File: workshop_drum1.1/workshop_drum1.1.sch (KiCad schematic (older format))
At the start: 30 parts, among them J1 9v_Battery_Clip, J2 Trigger_Input, J3 Output, U1 LM358, U2 7414, U3 78L05

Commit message: P1.1 - Updated footprints prior to deleting PCB
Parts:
- removed C?: 10uF, 4ms-footprints:Cap_Electrolytic_TH, symbol 4ms-passives:CAP-ELEC-TH
- removed SW?: SPDT_small, zfoot:Switch_Toggle_SPDT_Mini_SolderLug, symbol zMECH:SPDT_small
- added EnvelopeAndVoltageStarve1: PWRStrip, zfoot:BreadBoardStrip_4, symbol zMECH:GNDStrip
- added GND1: GNDStrip, zfoot:BreadBoardStripBold_4, symbol zMECH:GNDStrip
- added GND2: GNDStrip, zfoot:BreadBoardStripBold_7, symbol zMECH:GNDStrip
- added IN1, IN2, IN3, OUT1, OUT2, OUT3, PathToSwitch1: BreadBoardStrip, zfoot:BreadBoardStrip_4, symbol zMECH:BreadBoardStrip
- added Osc_Select1: SPDT_small, zfoot:Switch_Toggle_SPDT_Mini_SolderLug, symbol zMECH:SPDT_small
- added R10: 470 after pot on output, 4ms-footprints:Resistor_TH_300, symbol 4ms-passives:RTH
- added R9: 1k - trig input resistor, 4ms-footprints:Resistor_TH_300, symbol 4ms-passives:RTH
- C2: value 1uF -> 1uF or smaller?
- C5: value 220nF -> 100nf-220nF or bigger?
- DECAY1: value A500k-A1M -> A100k-A1M
- J2, J3: footprint zfoot:Jack_Instrument_Bigger -> zfoot:Jack_Instrument
- ON/OFF_LED1, Trig_LED1: footprint zfoot:LED_D5.0mm -> zfoot:LED_wired
- PITCH1: value B50k -> B50k- try with A100k
- R3: value 1k -> 1k smaller is brighter
- R4: value 1M -> SET THIS TO ADJUST SENSE
- R5: value 100k -> 100k before decay pot
- R6: value 470 -> 470 before pot on non-inv input
- R8: value 470 -> 470 smaller is brighter
- SENSE/STARVE1: value A50k -> A100k or bigger
- renumbered Button1 to Switch_On1
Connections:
- wire segments 63 -> 70
- no-connect marks 8 -> 2
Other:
- moved on the sheet: C2, C5, J3, R1, R7, Switch_On1, U1B

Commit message: P1.1 started working on breadboard strip
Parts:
- ON/OFF_LED1, Trig_LED1: footprint zfoot:LED_wired -> zfoot:LED_D5.0mm
- Switch_On1: footprint zfoot:SPST_Wired -> zfoot:Jack_Instrument_Bigger
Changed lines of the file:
@@
 F 0 "ON/OFF_LED1" H 2300 3496 45  0000 C CNN
 F 1 "LED-C1-A2" H 2300 3580 45  0000 C CNN
-F 2 "zfoot:LED_wired" H 2280 3850 20  0001 C CNN
+F 2 "zfoot:LED_D5.0mm" H 2280 3850 20  0001 C CNN
 F 3 "" H 2250 3700 60  0001 C CNN
 	1    2250 3700
@@
 F 0 "Switch_On1" H 1150 1100 60  0000 C CNN
 F 1 "SPST_small" H 1150 1050 20  0000 C CNN
-F 2 "zfoot:SPST_Wired" H 1150 1150 60  0001 C CNN
+F 2 "zfoot:Jack_Instrument_Bigger" H 1150 1150 60  0001 C CNN
 F 3 "" H 1150 1150 60  0001 C CNN
 	1    1150 1150
@@
 F 0 "Trig_LED1" H 6650 2596 45  0000 C CNN
 F 1 "LED-C1-A2" H 6650 2680 45  0000 C CNN
-F 2 "zfoot:LED_wired" H 6630 2950 20  0001 C CNN
+F 2 "zfoot:LED_D5.0mm" H 6630 2950 20  0001 C CNN
 F 3 "" H 6600 2800 60  0001 C CNN
 	1    6600 2800

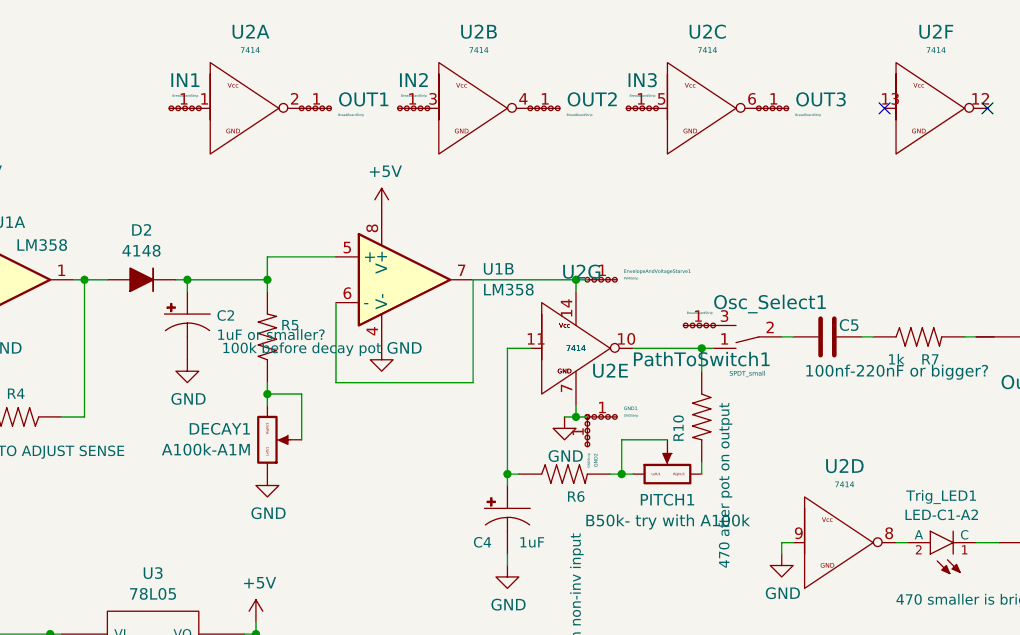
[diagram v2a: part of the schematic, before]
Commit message: re organizing boards with breakout footprints
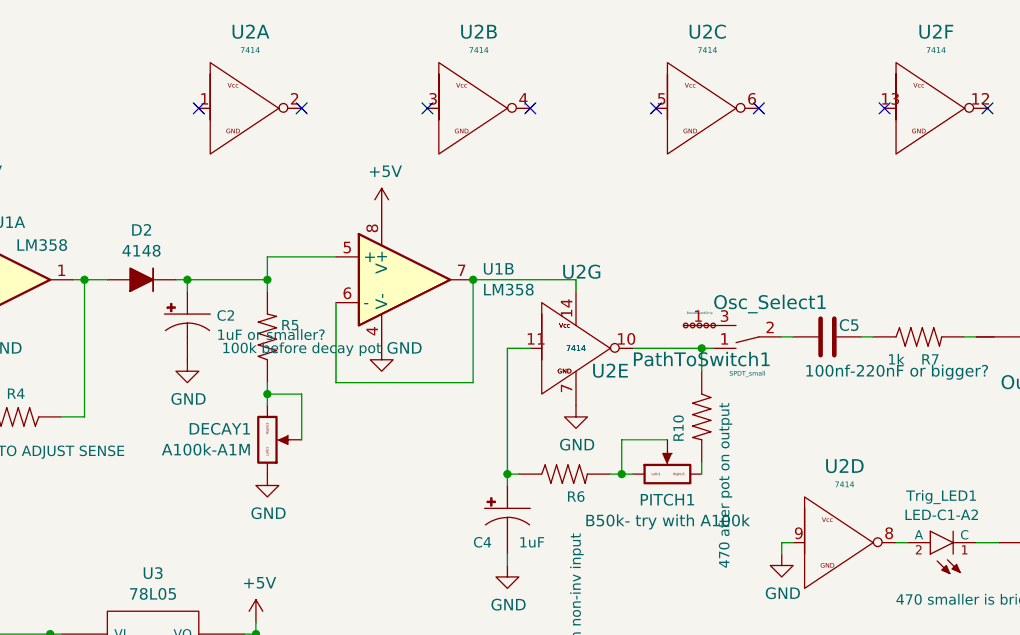
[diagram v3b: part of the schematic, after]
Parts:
- removed EnvelopeAndVoltageStarve1: PWRStrip, zfoot:BreadBoardStrip_4, symbol zMECH:GNDStrip
- removed GND1: GNDStrip, zfoot:BreadBoardStripBold_4, symbol zMECH:GNDStrip
- removed GND2: GNDStrip, zfoot:BreadBoardStripBold_7, symbol zMECH:GNDStrip
- removed IN1, IN2, IN3, OUT1, OUT2, OUT3: BreadBoardStrip, zfoot:BreadBoardStrip_4, symbol zMECH:BreadBoardStrip
- PathToSwitch1: footprint zfoot:BreadBoardStrip_4 -> zfoot:BREAKOUTswitch
- U2: footprint 4ms-footprints:DIP-14_W7.62mm -> zfoot:BREAKOUT
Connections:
- no-connect marks 2 -> 8
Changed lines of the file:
@@
 F 0 "U2" H 5100 1850 60  0000 C CNN
 F 1 "7414" H 4950 1950 25  0000 C CNN
-F 2 "4ms-footprints:DIP-14_W7.62mm" H 4900 2600 60  0001 C CNN
+F 2 "zfoot:BREAKOUT" H 4900 2600 60  0001 C CNN
 F 3 "" H 4900 2600 60  0001 C CNN
 	5    4950 1950
@@
 F 0 "U2" H 6125 3133 60  0000 C CNN
 F 1 "7414" H 6125 3054 25  0000 C CNN
-F 2 "4ms-footprints:DIP-14_W7.62mm" H 6050 3450 60  0001 C CNN
+F 2 "zfoot:BREAKOUT" H 6050 3450 60  0001 C CNN
 F 3 "" H 6050 3450 60  0001 C CNN
 	4    6100 2800
@@
 F 0 "U2" H 3525 1233 60  0000 C CNN
 F 1 "7414" H 3525 1154 25  0000 C CNN
-F 2 "4ms-footprints:DIP-14_W7.62mm" H 3450 1550 60  0001 C CNN
+F 2 "zfoot:BREAKOUT" H 3450 1550 60  0001 C CNN
 F 3 "" H 3450 1550 60  0001 C CNN
 	1    3500 900
@@
 F 0 "U2" H 5525 1233 60  0000 C CNN
 F 1 "7414" H 5525 1154 25  0000 C CNN
-F 2 "4ms-footprints:DIP-14_W7.62mm" H 5450 1550 60  0001 C CNN
+F 2 "zfoot:BREAKOUT" H 5450 1550 60  0001 C CNN
 F 3 "" H 5450 1550 60  0001 C CNN
 	3    5500 900
@@
 F 0 "U2" H 4525 1233 60  0000 C CNN
 F 1 "7414" H 4525 1154 25  0000 C CNN
-F 2 "4ms-footprints:DIP-14_W7.62mm" H 4450 1550 60  0001 C CNN
+F 2 "zfoot:BREAKOUT" H 4450 1550 60  0001 C CNN
 F 3 "" H 4450 1550 60  0001 C CNN
 	2    4500 900
@@
 F 0 "U2" H 6525 1233 60  0000 C CNN
 F 1 "7414" H 6525 1154 25  0000 C CNN
-F 2 "4ms-footprints:DIP-14_W7.62mm" H 6450 1550 60  0001 C CNN
+F 2 "zfoot:BREAKOUT" H 6450 1550 60  0001 C CNN
 F 3 "" H 6450 1550 60  0001 C CNN
 	6    6500 900
-	1    0    0    -1
-$EndComp
-$Comp
-L zMECH:BreadBoardStrip IN1
-U 1 1 5A32DFC0
-P 3300 900
-F 0 "IN1" H 3359 779 60  0000 C CNN
-F 1 "BreadBoardStrip" H 3359 845 10  0000 C CNN
-F 2 "zfoot:BreadBoardStrip_4" H 3170 880 60  0001 C CNN
-F 3 "" H 3300 900 60  0001 C CNN
-	1    3300 900
-	-1   0    0    1
-$EndComp
-$Comp
-L zMECH:BreadBoardStrip OUT1
-U 1 1 5A32E0DC
-P 3750 900
-F 0 "OUT1" H 3909 937 60  0000 L CNN
-F 1 "BreadBoardStrip" H 3909 871 10  0000 L CNN
-F 2 "zfoot:BreadBoardStrip_4" H 3620 880 60  0001 C CNN
-F 3 "" H 3750 900 60  0001 C CNN
-	1    3750 900
-	1    0    0    -1
-$EndComp
-$Comp
-L zMECH:BreadBoardStrip OUT3
-U 1 1 5A32E1BF
-P 5750 900
-F 0 "OUT3" H 5909 937 60  0000 L CNN
-F 1 "BreadBoardStrip" H 5909 871 10  0000 L CNN
-F 2 "zfoot:BreadBoardStrip_4" H 5620 880 60  0001 C CNN
-F 3 "" H 5750 900 60  0001 C CNN
-	1    5750 900
-	1    0    0    -1
-$EndComp
-$Comp
-L zMECH:BreadBoardStrip OUT2
-U 1 1 5A32E1FA
-P 4750 900
-F 0 "OUT2" H 4909 937 60  0000 L CNN
-F 1 "BreadBoardStrip" H 4909 871 10  0000 L CNN
-F 2 "zfoot:BreadBoardStrip_4" H 4620 880 60  0001 C CNN
-F 3 "" H 4750 900 60  0001 C CNN
-	1    4750 900
-	1    0    0    -1
-$EndComp
-$Comp
-L zMECH:BreadBoardStrip IN2
-U 1 1 5A32E61E
-P 4300 900
-F 0 "IN2" H 4359 779 60  0000 C CNN
-F 1 "BreadBoardStrip" H 4359 845 10  0000 C CNN
-F 2 "zfoot:BreadBoardStrip_4" H 4170 880 60  0001 C CNN
-F 3 "" H 4300 900 60  0001 C CNN
-	1    4300 900
-	-1   0    0    1
-$EndComp
-$Comp
-L zMECH:BreadBoardStrip IN3
-U 1 1 5A32E6B1
-P 5300 900
-F 0 "IN3" H 5359 779 60  0000 C CNN
-F 1 "BreadBoardStrip" H 5359 845 10  0000 C CNN
-F 2 "zfoot:BreadBoardStrip_4" H 5170 880 60  0001 C CNN
-F 3 "" H 5300 900 60  0001 C CNN
-	1    5300 900
-	-1   0    0    1
-$EndComp
-$Comp
-L zMECH:GNDStrip GND1
-U 1 1 5A32F5DA
-P 5000 2250
-F 0 "GND1" H 5159 2287 15  0000 L CNN
-F 1 "GNDStrip" H 5159 2256 10  0000 L CNN
-F 2 "zfoot:BreadBoardStripBold_4" H 4870 2230 60  0001 C CNN
-F 3 "" H 5000 2250 60  0001 C CNN
-	1    5000 2250
 	1    0    0    -1
 $EndComp
@@
 F 0 "U2" H 4975 2283 60  0000 C CNN
 F 1 "7414" H 4950 1950 25  0000 C CNN
-F 2 "4ms-footprints:DIP-14_W7.62mm" H 4900 2600 60  0001 C CNN
+F 2 "zfoot:BREAKOUT" H 4900 2600 60  0001 C CNN
 F 3 "" H 4900 2600 60  0001 C CNN
 	7    4950 1950
@@
 $EndComp
 Wire Wire Line
-	4950 1700 4950 1650
-Wire Wire Line
-	4500 1650 4950 1650
-Wire Wire Line
-	4950 2200 4950 2250
-Wire Wire Line
-	4950 2250 5000 2250
-Wire Wire Line
 	1600 3550 1600 3600
 Wire Wire Line
@@
 Wire Wire Line
 	4500 2100 4500 1650
-Connection ~ 4950 1650
 Wire Wire Line
 	4650 1950 4650 2500
@@
 F 0 "PathToSwitch1" H 5600 2000 60  0000 C CNN
 F 1 "BreadBoardStrip" H 5609 1795 10  0000 C CNN
-F 2 "zfoot:BreadBoardStrip_4" H 5420 1830 60  0001 C CNN
+F 2 "zfoot:BREAKOUTswitch" H 5420 1830 60  0001 C CNN
 F 3 "" H 5550 1850 60  0001 C CNN
 	1    5550 1850
 	-1   0    0    1
 $EndComp
-$Comp
-L zMECH:GNDStrip EnvelopeAndVoltageStarve1
-U 1 1 5A330F13
-P 5000 1650
-F 0 "EnvelopeAndVoltageStarve1" H 5159 1687 15  0000 L CNN
-F 1 "PWRStrip" H 5159 1656 10  0000 L CNN
-F 2 "zfoot:BreadBoardStrip_4" H 4870 1630 60  0001 C CNN
-F 3 "" H 5000 1650 60  0001 C CNN
-	1    5000 1650
-	1    0    0    -1
-$EndComp
 NoConn ~ 6300 900
 NoConn ~ 6750 900
-$Comp
-L zMECH:GNDStrip GND2
-U 1 1 5A336833
-P 5000 2250
-F 0 "GND2" H 5159 2287 15  0000 L CNN
-F 1 "GNDStrip" H 5159 2256 10  0000 L CNN
-F 2 "zfoot:BreadBoardStripBold_7" H 4870 2230 60  0001 C CNN
-F 3 "" H 5000 2250 60  0001 C CNN
-	1    5000 2250
-	0    1    1    0
-$EndComp
 Wire Wire Line
 	2000 3200 2050 3200
@@
 Wire Wire Line
 	3600 1650 3600 1700
-Wire Wire Line
-	4950 1650 5000 1650
 Wire Wire Line
 	4650 2500 4650 2550
@@
 L 4ms-power:GND #PWR0101
 U 1 1 5ABB579D
-P 4900 2250
-F 0 "#PWR0101" H 4900 2000 50  0001 C CNN
-F 1 "GND" H 4905 2077 50  0000 C CNN
-F 2 "" H 4900 2250 50  0001 C CNN
-F 3 "" H 4900 2250 50  0001 C CNN
-	1    4900 2250
-	1    0    0    -1
-$EndComp
-Wire Wire Line
-	4900 2250 4950 2250
-Connection ~ 4950 2250
+P 4950 2200
+F 0 "#PWR0101" H 4950 1950 50  0001 C CNN
+F 1 "GND" H 4955 2027 50  0000 C CNN
+F 2 "" H 4950 2200 50  0001 C CNN
+F 3 "" H 4950 2200 50  0001 C CNN
+	1    4950 2200
+	1    0    0    -1
+$EndComp
 Wire Wire Line
 	1000 1150 750  1150
@@
 Wire Wire Line
 	5500 2450 5500 2500
+Wire Wire Line
+	4500 1650 4950 1650
+Wire Wire Line
+	4950 1650 4950 1700
+Connection ~ 4500 1650
+NoConn ~ 3300 900
+NoConn ~ 3750 900
+NoConn ~ 4300 900
+NoConn ~ 4750 900
+NoConn ~ 5300 900
+NoConn ~ 5750 900
 $EndSCHEMATC

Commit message: starting to lay traces
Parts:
- added R11: 1k, 4ms-footprints:Resistor_TH_300, symbol 4ms-passives:RTH
- C1: value 100uF -> 10uF
- J1: footprint zfoot:Jack_DC -> zfoot:Jack_Instrument_Bigger
- J2, J3: footprint zfoot:Jack_Instrument -> zfoot:Jack_Instrument_Bigger
- U1: footprint 4ms-footprints:DIP_8pin_TL082_TH -> zfoot:DIP_8pin_TL082_TH_CenteredNotOnPin1
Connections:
- net at D2.2 (A), R4.1: now also U1.7; no longer U1.1
- net at R2.1, R4.2: now also U1.6 (-); no longer U1.2 (-)
- net at SENSE/STARVE1.2 (Center): now also U1.5 (+); no longer U1.3 (+)
- net at C2.1 (+), D2.1 (K): now also R5.1, U1.3 (+); no longer R5.2, U1.5 (+)
- net at R10.1, U2.10: now also R11.2; no longer Osc_Select1.1
- net at DECAY1.2 (Center), DECAY1.3 (Right): now also R5.2; no longer R5.1
- new net: U1.1, U1.2 (-), U2.14
- new net: Osc_Select1.1, R11.1
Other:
- moved on the sheet: C5, J3, Osc_Select1, PathToSwitch1, R7
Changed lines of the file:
@@
 $Comp
 L linear1:LM358 U1
-U 1 1 5A324A57
+U 2 1 5A324A57
 P 2450 1650
 F 0 "U1" H 2400 1900 50  0000 L CNN
 F 1 "LM358" H 2500 1800 50  0000 L CNN
-F 2 "4ms-footprints:DIP_8pin_TL082_TH" H 2450 1650 50  0001 C CNN
+F 2 "zfoot:DIP_8pin_TL082_TH_CenteredNotOnPin1" H 2450 1650 50  0001 C CNN
 F 3 "" H 2450 1650 50  0001 C CNN
-	1    2450 1650
+	2    2450 1650
 	1    0    0    -1
 $EndComp
 $Comp
 L linear1:LM358 U1
-U 2 1 5A324B18
+U 1 1 5A324B18
 P 4200 1650
 F 0 "U1" H 4541 1696 50  0000 L CNN
 F 1 "LM358" H 4541 1605 50  0000 L CNN
-F 2 "4ms-footprints:DIP_8pin_TL082_TH" H 4200 1650 50  0001 C CNN
+F 2 "zfoot:DIP_8pin_TL082_TH_CenteredNotOnPin1" H 4200 1650 50  0001 C CNN
 F 3 "" H 4200 1650 50  0001 C CNN
-	2    4200 1650
+	1    4200 1650
 	1    0    0    -1
 $EndComp
@@
 F 0 "J1" H 1131 3837 60  0000 C CNN
 F 1 "9v_Battery_Clip" H 1131 3731 60  0000 C CNN
-F 2 "zfoot:Jack_DC" H 1100 3400 60  0001 C CNN
+F 2 "zfoot:Jack_Instrument_Bigger" H 1100 3400 60  0001 C CNN
 F 3 "" H 1100 3400 60  0001 C CNN
 	1    1100 3400
@@
 P 2650 3350
 F 0 "C1" H 2778 3342 45  0000 L CNN
-F 1 "100uF" H 2778 3258 45  0000 L CNN
+F 1 "10uF" H 2778 3258 45  0000 L CNN
 F 2 "4ms-footprints:Cap_Electrolytic_TH" H 2680 3500 20  0001 C CNN
 F 3 "" H 2650 3350 60  0001 C CNN
@@
 L 4ms-passives:CAP_TH C5
 U 1 1 5A3339E6
-P 6050 1900
-F 0 "C5" V 6000 1950 50  0000 L CNN
-F 1 "100nf-220nF or bigger?" V 6200 1800 50  0000 L CNN
-F 2 "4ms-footprints:Cap_Ceramic_TH" H 6088 1750 50  0001 C CNN
-F 3 "" H 6050 1900 50  0001 C CNN
-	1    6050 1900
+P 6400 1900
+F 0 "C5" V 6350 1950 50  0000 L CNN
+F 1 "100nf-220nF or bigger?" V 6550 1800 50  0000 L CNN
+F 2 "4ms-footprints:Cap_Ceramic_TH" H 6438 1750 50  0001 C CNN
+F 3 "" H 6400 1900 50  0001 C CNN
+	1    6400 1900
 	0    1    1    0
 $EndComp
@@
 L zMECH:SPDT_small Osc_Select1
 U 1 1 5A3358B6
-P 5700 1900
-F 0 "Osc_Select1" H 5600 1750 60  0000 C CNN
-F 1 "SPDT_small" H 5700 2060 20  0000 C CNN
-F 2 "zfoot:Switch_Toggle_SPDT_Mini_SolderLug" H 5700 1900 60  0001 C CNN
-F 3 "" H 5700 1900 60  0001 C CNN
-	1    5700 1900
+P 6100 1900
+F 0 "Osc_Select1" H 6000 1750 60  0000 C CNN
+F 1 "SPDT_small" H 6100 2060 20  0000 C CNN
+F 2 "zfoot:Switch_Toggle_SPDT_Mini_SolderLug" H 6100 1900 60  0001 C CNN
+F 3 "" H 6100 1900 60  0001 C CNN
+	1    6100 1900
 	-1   0    0    1
 $EndComp
@@
 F 0 "J2" H 650 1600 60  0000 C CNN
 F 1 "Trigger_Input" H 1100 1450 60  0000 C CNN
-F 2 "zfoot:Jack_Instrument" H 900 1500 60  0001 C CNN
+F 2 "zfoot:Jack_Instrument_Bigger" H 900 1500 60  0001 C CNN
 F 3 "" H 900 1500 60  0000 C CNN
 	1    900  1500
@@
 F 3 "" H 3600 1900 60  0001 C CNN
 	1    3600 1900
-	0    -1   -1   0
+	0    1    1    0
 $EndComp
 $Comp
@@
 Wire Wire Line
 	5150 2350 5350 2350
-Wire Wire Line
-	5850 1900 5900 1900
 $Comp
 L 4ms-passives:RTH R7
 U 1 1 5A33161A
-P 6450 1900
-F 0 "R7" H 6500 1800 45  0000 C CNN
-F 1 "1k" H 6350 1800 45  0000 C CNN
-F 2 "4ms-footprints:Resistor_TH_300" H 6480 2050 20  0001 C CNN
-F 3 "" H 6450 1900 60  0001 C CNN
-	1    6450 1900
-	1    0    0    -1
-$EndComp
-Wire Wire Line
-	6200 1900 6250 1900
+P 6750 1900
+F 0 "R7" H 6800 1800 45  0000 C CNN
+F 1 "1k" H 6650 1800 45  0000 C CNN
+F 2 "4ms-footprints:Resistor_TH_300" H 6780 2050 20  0001 C CNN
+F 3 "" H 6750 1900 60  0001 C CNN
+	1    6750 1900
+	1    0    0    -1
+$EndComp
 $Comp
 L zMECH:JACK-TIP_GND J3
 U 1 1 5A331971
-P 7150 2050
-F 0 "J3" H 6900 2150 60  0000 C CNN
-F 1 "Output" H 7350 2000 60  0000 C CNN
-F 2 "zfoot:Jack_Instrument" H 7150 2050 60  0001 C CNN
-F 3 "" H 7150 2050 60  0000 C CNN
-	1    7150 2050
+P 7450 2050
+F 0 "J3" H 7200 2150 60  0000 C CNN
+F 1 "Output" H 7650 2000 60  0000 C CNN
+F 2 "zfoot:Jack_Instrument_Bigger" H 7450 2050 60  0001 C CNN
+F 3 "" H 7450 2050 60  0000 C CNN
+	1    7450 2050
 	-1   0    0    -1
 $EndComp
 Wire Wire Line
-	6650 1900 6700 1900
+	6950 1900 7000 1900
 $Comp
 L 4ms-power:GND #PWR018
 U 1 1 5A331D26
-P 7300 2200
-F 0 "#PWR018" H 7300 1950 50  0001 C CNN
-F 1 "GND" H 7305 2027 50  0000 C CNN
-F 2 "" H 7300 2200 50  0001 C CNN
-F 3 "" H 7300 2200 50  0001 C CNN
-	1    7300 2200
-	1    0    0    -1
-$EndComp
-Wire Wire Line
-	7300 2150 7300 2200
+P 7600 2200
+F 0 "#PWR018" H 7600 1950 50  0001 C CNN
+F 1 "GND" H 7605 2027 50  0000 C CNN
+F 2 "" H 7600 2200 50  0001 C CNN
+F 3 "" H 7600 2200 50  0001 C CNN
+	1    7600 2200
+	1    0    0    -1
+$EndComp
+Wire Wire Line
+	7600 2150 7600 2200
 $Comp
 L 4ms-power:GND #PWR019
@@
 L zMECH:BreadBoardStrip PathToSwitch1
 U 1 1 5A33DD61
-P 5550 1850
-F 0 "PathToSwitch1" H 5600 2000 60  0000 C CNN
-F 1 "BreadBoardStrip" H 5609 1795 10  0000 C CNN
-F 2 "zfoot:BREAKOUTswitch" H 5420 1830 60  0001 C CNN
-F 3 "" H 5550 1850 60  0001 C CNN
-	1    5550 1850
+P 5950 1850
+F 0 "PathToSwitch1" H 6000 2000 60  0000 C CNN
+F 1 "BreadBoardStrip" H 6009 1795 10  0000 C CNN
+F 2 "zfoot:BREAKOUTswitch" H 5820 1830 60  0001 C CNN
+F 3 "" H 5950 1850 60  0001 C CNN
+	1    5950 1850
 	-1   0    0    1
 $EndComp
@@
 Wire Wire Line
 	1800 1350 1800 1400
-Wire Wire Line
-	5200 1950 5500 1950
 $Comp
 L 4ms-passives:RTH R10
@@
 $EndComp
 Wire Wire Line
-	5500 1950 5500 2050
-Connection ~ 5500 1950
-Wire Wire Line
-	5500 1950 5550 1950
-Wire Wire Line
 	5500 2450 5500 2500
 Wire Wire Line
@@
 NoConn ~ 5300 900
 NoConn ~ 5750 900
+$Comp
+L 4ms-passives:RTH R11
+U 1 1 5AC19556
+P 5750 1950
+F 0 "R11" H 5800 1850 45  0000 C CNN
+F 1 "1k" H 6050 2050 45  0000 C CNN
+F 2 "4ms-footprints:Resistor_TH_300" H 5780 2100 20  0001 C CNN
+F 3 "" H 5750 1950 60  0001 C CNN
+	1    5750 1950
+	-1   0    0    1
+$EndComp
+Wire Wire Line
+	5550 1950 5500 1950
+Wire Wire Line
+	5500 2050 5500 1950
+Connection ~ 5500 1950
+Wire Wire Line
+	5500 1950 5200 1950
 $EndSCHEMATC

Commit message: Ready for review
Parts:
- renumbered Switch_On1 to Button1
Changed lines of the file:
@@
 $EndComp
 $Comp
-L zMECH:SPST_small Switch_On1
+L zMECH:SPST_small Button1
 U 1 1 5A33654C
 P 1150 1150
-F 0 "Switch_On1" H 1150 1100 60  0000 C CNN
+F 0 "Button1" H 1150 1100 60  0000 C CNN
 F 1 "SPST_small" H 1150 1050 20  0000 C CNN
 F 2 "zfoot:Jack_Instrument_Bigger" H 1150 1150 60  0001 C CNN
